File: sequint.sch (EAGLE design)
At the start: 65 parts, among them IC1 STM32F10XCXT6, Q1 MOSFET-NCHANNELSMD, Q2 MOSFET-NCHANNELSMD, Q3 MOSFET-NCHANNELSMD, Q4 MOSFET-NCHANNELSMD, Q5 16MHz, U1 LSM330DLCTRLGA, U2 MCP73831, U4 NRF24L01SMD

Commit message: Fix routing
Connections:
- removed net IRQ: JPRF-A.1
- removed net N$1: D1.A, D2.A, D3.A, D4.A, Q1.S, Q2.S, Q3.S, Q4.S
- net GND: now also D1.A, D2.A, D3.A, D4.A, Q1.S, Q2.S, Q3.S, Q4.S
- net NRF-IRQ: now also JPRF-A.1
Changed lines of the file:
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@@
 </variantdefs>
 <classes>
-<class number="0" name="default" width="0" drill="0">
+<class number="0" name="default" width="0.254" drill="0">
+<clearance class="0" value="0.254"/>
 </class>
 </classes>
@@
 <pinref part="U4" gate="G$1" pin="IRQ"/>
 </segment>
-</net>
-<net name="IRQ" class="0">
 <segment>
 <pinref part="JPRF-A" gate="A" pin="1"/>
@@
 </busses>
 <nets>
-<net name="N$1" class="0">
+<net name="VL-4" class="0">
+<segment>
+<pinref part="D4" gate="G$1" pin="C"/>
+<pinref part="Q4" gate="G$1" pin="D"/>
+<wire x1="96.52" y1="50.8" x2="96.52" y2="53.34" width="0" layer="91"/>
+<wire x1="96.52" y1="53.34" x2="88.9" y2="53.34" width="0" layer="91"/>
+<wire x1="88.9" y1="53.34" x2="88.9" y2="54.61" width="0" layer="91"/>
+<junction x="88.9" y="53.34"/>
+<pinref part="MOT4" gate="G$1" pin="1"/>
+<wire x1="88.9" y1="53.34" x2="88.9" y2="60.96" width="0" layer="91"/>
+</segment>
+</net>
+<net name="VL-3" class="0">
+<segment>
+<pinref part="D3" gate="G$1" pin="C"/>
+<pinref part="Q3" gate="G$1" pin="D"/>
+<wire x1="73.66" y1="50.8" x2="73.66" y2="53.34" width="0" layer="91"/>
+<wire x1="73.66" y1="53.34" x2="66.04" y2="53.34" width="0" layer="91"/>
+<wire x1="66.04" y1="53.34" x2="66.04" y2="54.61" width="0" layer="91"/>
+<junction x="66.04" y="53.34"/>
+<pinref part="MOT3" gate="G$1" pin="2"/>
+<wire x1="66.04" y1="60.96" x2="66.04" y2="53.34" width="0" layer="91"/>
+</segment>
+</net>
+<net name="VL-2" class="0">
+<segment>
+<pinref part="D2" gate="G$1" pin="C"/>
+<pinref part="Q2" gate="G$1" pin="D"/>
+<wire x1="50.8" y1="50.8" x2="50.8" y2="53.34" width="0" layer="91"/>
+<wire x1="50.8" y1="53.34" x2="43.18" y2="53.34" width="0" layer="91"/>
+<wire x1="43.18" y1="53.34" x2="43.18" y2="54.61" width="0" layer="91"/>
+<junction x="43.18" y="53.34"/>
+<pinref part="MOT2" gate="G$1" pin="1"/>
+<wire x1="43.18" y1="60.96" x2="43.18" y2="53.34" width="0" layer="91"/>
+</segment>
+</net>
+<net name="VL-1" class="0">
+<segment>
+<pinref part="D1" gate="G$1" pin="C"/>
+<pinref part="Q1" gate="G$1" pin="D"/>
+<wire x1="30.48" y1="50.8" x2="30.48" y2="53.34" width="0" layer="91"/>
+<wire x1="30.48" y1="53.34" x2="22.86" y2="53.34" width="0" layer="91"/>
+<wire x1="22.86" y1="53.34" x2="22.86" y2="54.61" width="0" layer="91"/>
+<junction x="22.86" y="53.34"/>
+<pinref part="MOT1" gate="G$1" pin="2"/>
+<wire x1="22.86" y1="53.34" x2="22.86" y2="60.96" width="0" layer="91"/>
+</segment>
+</net>
+<net name="GND" class="0">
+<segment>
+<pinref part="CN1" gate="G$1" pin="GND"/>
+<wire x1="20.32" y1="2.54" x2="22.86" y2="2.54" width="0" layer="91"/>
+<label x="22.86" y="2.54" size="1.778" layer="95"/>
+</segment>
+<segment>
+<pinref part="U2" gate="G$1" pin="VSS"/>
+<wire x1="91.44" y1="7.62" x2="106.68" y2="7.62" width="0" layer="91"/>
+<pinref part="R5" gate="G$1" pin="2"/>
+<wire x1="104.14" y1="10.16" x2="106.68" y2="10.16" width="0" layer="91"/>
+<wire x1="106.68" y1="10.16" x2="106.68" y2="7.62" width="0" layer="91"/>
+<pinref part="C7" gate="G$1" pin="P$2"/>
+<wire x1="106.68" y1="12.7" x2="106.68" y2="10.16" width="0" layer="91"/>
+<pinref part="3.3VREG" gate="G$1" pin="GND"/>
+<wire x1="106.68" y1="10.16" x2="134.62" y2="10.16" width="0" layer="91"/>
+<wire x1="134.62" y1="10.16" x2="134.62" y2="20.32" width="0" layer="91"/>
+<wire x1="134.62" y1="20.32" x2="132.08" y2="20.32" width="0" layer="91"/>
+<junction x="106.68" y="10.16"/>
+<label x="134.62" y="10.16" size="1.778" layer="95"/>
+</segment>
+<segment>
+<pinref part="PWR" gate="A" pin="5"/>
+<wire x1="114.3" y1="35.56" x2="114.3" y2="33.02" width="0" layer="91"/>
+<wire x1="114.3" y1="33.02" x2="119.38" y2="33.02" width="0" layer="91"/>
+<label x="119.38" y="33.02" size="1.778" layer="95"/>
+</segment>
+<segment>
+<pinref part="RN1" gate="B" pin="1"/>
+<pinref part="RN1" gate="D" pin="1"/>
+<wire x1="139.7" y1="45.72" x2="144.78" y2="45.72" width="0" layer="91"/>
+<wire x1="144.78" y1="45.72" x2="149.86" y2="45.72" width="0" layer="91"/>
+<wire x1="144.78" y1="45.72" x2="144.78" y2="43.18" width="0" layer="91"/>
+<label x="144.78" y="43.18" size="1.778" layer="95" rot="R180"/>
+</segment>
 <segment>
 <pinref part="Q1" gate="G$1" pin="S"/>
@@
 <junction x="66.04" y="38.1"/>
 <junction x="43.18" y="38.1"/>
-</segment>
-</net>
-<net name="VL-4" class="0">
-<segment>
-<pinref part="D4" gate="G$1" pin="C"/>
-<pinref part="Q4" gate="G$1" pin="D"/>
-<wire x1="96.52" y1="50.8" x2="96.52" y2="53.34" width="0" layer="91"/>
-<wire x1="96.52" y1="53.34" x2="88.9" y2="53.34" width="0" layer="91"/>
-<wire x1="88.9" y1="53.34" x2="88.9" y2="54.61" width="0" layer="91"/>
-<junction x="88.9" y="53.34"/>
-<pinref part="MOT4" gate="G$1" pin="1"/>
-<wire x1="88.9" y1="53.34" x2="88.9" y2="60.96" width="0" layer="91"/>
-</segment>
-</net>
-<net name="VL-3" class="0">
-<segment>
-<pinref part="D3" gate="G$1" pin="C"/>
-<pinref part="Q3" gate="G$1" pin="D"/>
-<wire x1="73.66" y1="50.8" x2="73.66" y2="53.34" width="0" layer="91"/>
-<wire x1="73.66" y1="53.34" x2="66.04" y2="53.34" width="0" layer="91"/>
-<wire x1="66.04" y1="53.34" x2="66.04" y2="54.61" width="0" layer="91"/>
-<junction x="66.04" y="53.34"/>
-<pinref part="MOT3" gate="G$1" pin="2"/>
-<wire x1="66.04" y1="60.96" x2="66.04" y2="53.34" width="0" layer="91"/>
-</segment>
-</net>
-<net name="VL-2" class="0">
-<segment>
-<pinref part="D2" gate="G$1" pin="C"/>
-<pinref part="Q2" gate="G$1" pin="D"/>
-<wire x1="50.8" y1="50.8" x2="50.8" y2="53.34" width="0" layer="91"/>
-<wire x1="50.8" y1="53.34" x2="43.18" y2="53.34" width="0" layer="91"/>
-<wire x1="43.18" y1="53.34" x2="43.18" y2="54.61" width="0" layer="91"/>
-<junction x="43.18" y="53.34"/>
-<pinref part="MOT2" gate="G$1" pin="1"/>
-<wire x1="43.18" y1="60.96" x2="43.18" y2="53.34" width="0" layer="91"/>
-</segment>
-</net>
-<net name="VL-1" class="0">
-<segment>
-<pinref part="D1" gate="G$1" pin="C"/>
-<pinref part="Q1" gate="G$1" pin="D"/>
-<wire x1="30.48" y1="50.8" x2="30.48" y2="53.34" width="0" layer="91"/>
-<wire x1="30.48" y1="53.34" x2="22.86" y2="53.34" width="0" layer="91"/>
-<wire x1="22.86" y1="53.34" x2="22.86" y2="54.61" width="0" layer="91"/>
-<junction x="22.86" y="53.34"/>
-<pinref part="MOT1" gate="G$1" pin="2"/>
-<wire x1="22.86" y1="53.34" x2="22.86" y2="60.96" width="0" layer="91"/>
-</segment>
-</net>
-<net name="GND" class="0">
-<segment>
-<pinref part="CN1" gate="G$1" pin="GND"/>
-<wire x1="20.32" y1="2.54" x2="22.86" y2="2.54" width="0" layer="91"/>
-<label x="22.86" y="2.54" size="1.778" layer="95"/>
-</segment>
-<segment>
-<pinref part="U2" gate="G$1" pin="VSS"/>
-<wire x1="91.44" y1="7.62" x2="106.68" y2="7.62" width="0" layer="91"/>
-<pinref part="R5" gate="G$1" pin="2"/>
-<wire x1="104.14" y1="10.16" x2="106.68" y2="10.16" width="0" layer="91"/>
-<wire x1="106.68" y1="10.16" x2="106.68" y2="7.62" width="0" layer="91"/>
-<pinref part="C7" gate="G$1" pin="P$2"/>
-<wire x1="106.68" y1="12.7" x2="106.68" y2="10.16" width="0" layer="91"/>
-<pinref part="3.3VREG" gate="G$1" pin="GND"/>
-<wire x1="106.68" y1="10.16" x2="134.62" y2="10.16" width="0" layer="91"/>
-<wire x1="134.62" y1="10.16" x2="134.62" y2="20.32" width="0" layer="91"/>
-<wire x1="134.62" y1="20.32" x2="132.08" y2="20.32" width="0" layer="91"/>
-<junction x="106.68" y="10.16"/>
-<label x="134.62" y="10.16" size="1.778" layer="95"/>
-</segment>
-<segment>
-<pinref part="PWR" gate="A" pin="5"/>
-<wire x1="114.3" y1="35.56" x2="114.3" y2="33.02" width="0" layer="91"/>
-<wire x1="114.3" y1="33.02" x2="119.38" y2="33.02" width="0" layer="91"/>
-<label x="119.38" y="33.02" size="1.778" layer="95"/>
-</segment>
-<segment>
-<pinref part="RN1" gate="B" pin="1"/>
-<pinref part="RN1" gate="D" pin="1"/>
-<wire x1="139.7" y1="45.72" x2="144.78" y2="45.72" width="0" layer="91"/>
-<wire x1="144.78" y1="45.72" x2="149.86" y2="45.72" width="0" layer="91"/>
-<wire x1="144.78" y1="45.72" x2="144.78" y2="43.18" width="0" layer="91"/>
-<label x="144.78" y="43.18" size="1.778" layer="95" rot="R180"/>
-</segment>
-</net>
+<label x="25.4" y="38.1" size="1.778" layer="95"/>
+</segment>
+</net>

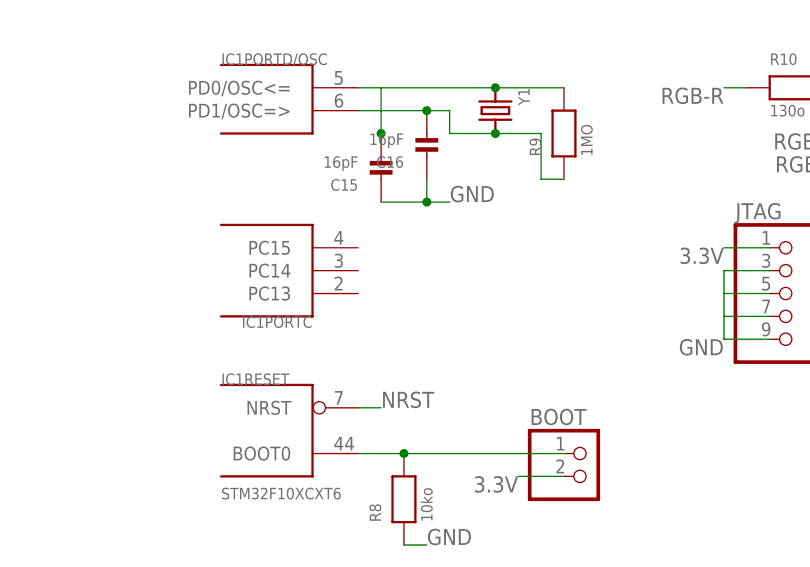
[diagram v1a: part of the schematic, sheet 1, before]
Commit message: Break out portC
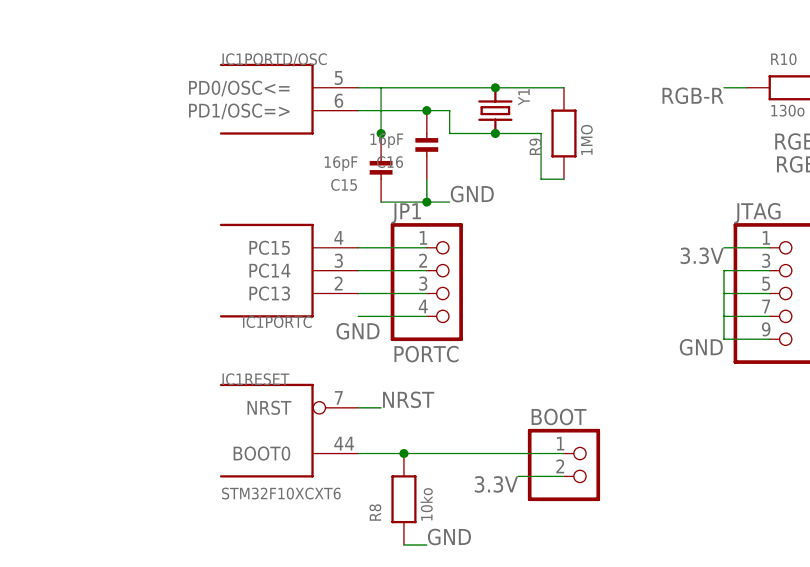
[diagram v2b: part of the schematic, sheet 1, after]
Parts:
- added JP1: PORTC, nonolith:HEADER-1X4ROUND
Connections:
- new net N$1: IC1PORTC.PC15, JP1.1
- new net N$4: IC1PORTC.PC14, JP1.2
- new net N$6: IC1PORTC.PC13, JP1.3
- net GND: now also JP1.4
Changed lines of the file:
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@@
 <part name="LED1" library="microbuilder" deviceset="LED_RGB_PLCC6" device="CREE-CLV6A"/>
 <part name="R10" library="nonolith" deviceset="RESISTOR" device="0603" value="130o"/>
+<part name="JP1" library="nonolith" deviceset="HEADER-1X4" device="ROUND" value="PORTC"/>
 </parts>
 <sheets>
@@
 <instance part="LED1" gate="G$1" x="83.82" y="38.1"/>
 <instance part="R10" gate="G$1" x="63.5" y="43.18"/>
+<instance part="JP1" gate="A" x="25.4" y="20.32"/>
 </instances>
 <busses>
@@
 <wire x1="99.06" y1="38.1" x2="99.06" y2="40.64" width="0" layer="91"/>
 </segment>
+<segment>
+<pinref part="JP1" gate="A" pin="4"/>
+<wire x1="22.86" y1="17.78" x2="15.24" y2="17.78" width="0.1524" layer="91"/>
+<label x="12.7" y="15.24" size="1.778" layer="95"/>
+</segment>
 </net>
 <net name="3.3V" class="0">
@@
 </segment>
 </net>
+<net name="N$1" class="0">
+<segment>
+<pinref part="IC1" gate="PORTC" pin="PC15"/>
+<pinref part="JP1" gate="A" pin="1"/>
+<wire x1="15.24" y1="25.4" x2="22.86" y2="25.4" width="0.1524" layer="91"/>
+</segment>
+</net>
+<net name="N$4" class="0">
+<segment>
+<pinref part="IC1" gate="PORTC" pin="PC14"/>
+<wire x1="15.24" y1="22.86" x2="22.86" y2="22.86" width="0.1524" layer="91"/>
+<pinref part="JP1" gate="A" pin="2"/>
+</segment>
+</net>
+<net name="N$6" class="0">
+<segment>
+<pinref part="IC1" gate="PORTC" pin="PC13"/>
+<pinref part="JP1" gate="A" pin="3"/>
+<wire x1="15.24" y1="20.32" x2="22.86" y2="20.32" width="0.1524" layer="91"/>
+</segment>
+</net>

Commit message: Silkscreen
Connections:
- net N$1 renamed PC15
- net N$4 renamed PC14
- net N$6 renamed PC13
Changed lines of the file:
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@@
 </segment>
 </net>
-<net name="N$1" class="0">
+<net name="PC15" class="0">
 <segment>
 <pinref part="IC1" gate="PORTC" pin="PC15"/>
@@
 </segment>
 </net>
-<net name="N$4" class="0">
+<net name="PC14" class="0">
 <segment>
 <pinref part="IC1" gate="PORTC" pin="PC14"/>
@@
 </segment>
 </net>
-<net name="N$6" class="0">
+<net name="PC13" class="0">
 <segment>
 <pinref part="IC1" gate="PORTC" pin="PC13"/>
